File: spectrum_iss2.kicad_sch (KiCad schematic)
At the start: 185 parts, among them IC1 ULA, IC10 4116, IC11 4116, IC12 4116, IC13 4116, IC14 LM1889, IC15 4532, IC16 4532, IC17 4532, IC18 4532, IC19 4532, IC2 Z80, IC20 4532, IC21 4532, IC22 4532, IC23 74LS32, IC24 74LS00, IC25 74LS157, IC26 74LS157, IC3 74LS157, IC4 74LS157, IC5 ROM, IC6 4116, IC7 4116, IC8 4116, IC9 4116, J1 MIC, J2 EAR, J3 EDGE CONNECTOR, J4 Barrel_Jack, T1 COIL 13/39, U1 MODULATOR, U2 L7805, X1 18MHz, X2 4.433MHz

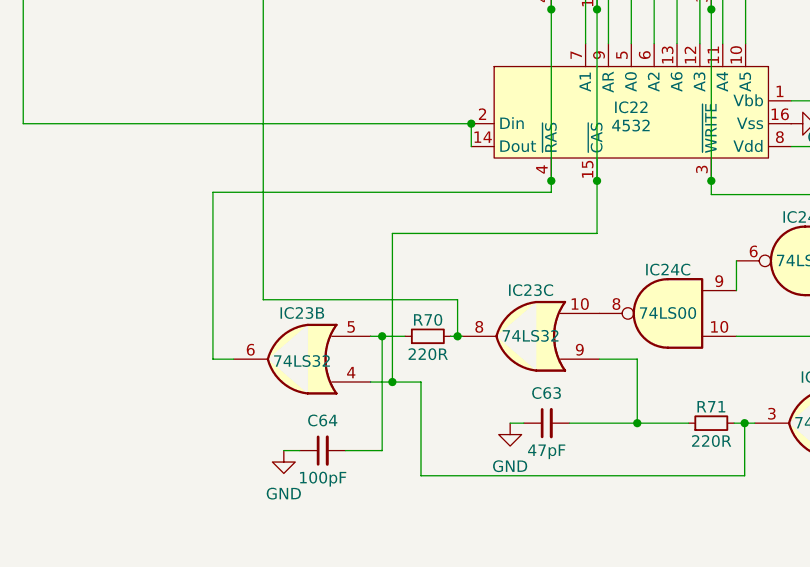
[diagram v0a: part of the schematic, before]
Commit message: fix reversed wiring of RAS and CAS on IC23
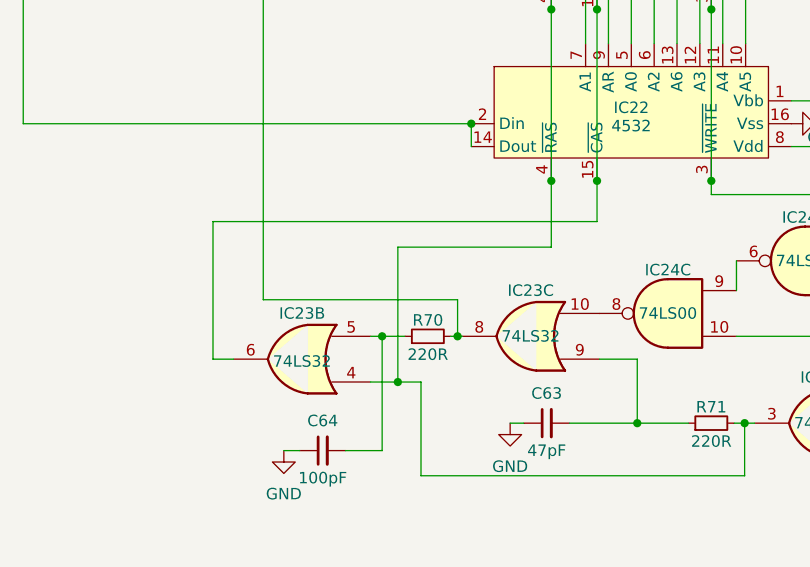
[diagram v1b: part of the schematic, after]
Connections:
- net at IC15.15 (~{CAS}), IC16.15 (~{CAS}), IC17.15 (~{CAS})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: now also IC23.6; no longer IC23.3, IC23.4, R71.2
- net at IC15.4 (~{RAS}), IC16.4 (~{RAS}), IC17.4 (~{RAS})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: now also IC23.3, IC23.4, R71.2; no longer IC23.6
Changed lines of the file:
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@@
   (junction (at 363.728 328.168) (diameter 0) (color 0 0 0 0)
   )
+  (junction (at 571.214 454.406) (diameter 0) (color 0 0 0 0)
+  )
   (junction (at 233.934 203.962) (diameter 0) (color 0 0 0 0)
   )
@@
   (junction (at 467.868 253.238) (diameter 0) (color 0 0 0 0)
   )
-  (junction (at 570.6089 454.406) (diameter 0) (color 0 0 0 0)
-  )
   (junction (at 169.926 271.526) (diameter 0) (color 0 0 0 0)
   )
@@
     (stroke (width 0) (type default))
   )
+  (wire (pts (xy 550.6743 436.5786) (xy 550.6743 451.866))
+    (stroke (width 0) (type default))
+  )
   (wire (pts (xy 535.686 146.812) (xy 535.686 148.844))
     (stroke (width 0) (type default))
@@
     (stroke (width 0) (type default))
   )
-  (wire (pts (xy 570.6089 454.406) (xy 568.198 454.406))
-    (stroke (width 0) (type default))
-  )
   (wire (pts (xy 225.552 255.27) (xy 219.202 255.27))
     (stroke (width 0) (type default))
@@
     (stroke (width 0) (type default))
   )
+  (wire (pts (xy 588.264 432.054) (xy 588.264 439.42))
+    (stroke (width 0) (type default))
+  )
   (wire (pts (xy 614.68 242.57) (xy 614.68 168.402))
     (stroke (width 0) (type default))
   )
+  (wire (pts (xy 571.214 439.42) (xy 571.214 454.406))
+    (stroke (width 0) (type default))
+  )
   (wire (pts (xy 343.408 320.802) (xy 343.408 335.28))
     (stroke (width 0) (type default))
@@
     (stroke (width 0) (type default))
   )
-  (wire (pts (xy 550.672 433.324) (xy 588.264 433.324))
-    (stroke (width 0) (type default))
-  )
   (wire (pts (xy 333.248 305.816) (xy 333.248 320.802))
     (stroke (width 0) (type default))
@@
     (stroke (width 0) (type default))
   )
+  (wire (pts (xy 588.264 439.42) (xy 571.214 439.42))
+    (stroke (width 0) (type default))
+  )
   (wire (pts (xy 225.552 202.184) (xy 225.552 203.962))
     (stroke (width 0) (type default))
@@
     (stroke (width 0) (type default))
   )
+  (wire (pts (xy 593.344 436.5786) (xy 550.6743 436.5786))
+    (stroke (width 0) (type default))
+  )
   (wire (pts (xy 542.036 348.234) (xy 579.374 348.234))
     (stroke (width 0) (type default))
@@
     (stroke (width 0) (type default))
   )
+  (wire (pts (xy 571.214 454.406) (xy 573.786 454.406))
+    (stroke (width 0) (type default))
+  )
   (wire (pts (xy 233.172 226.822) (xy 226.314 226.822))
     (stroke (width 0) (type default))
@@
     (stroke (width 0) (type default))
   )
-  (wire (pts (xy 552.958 451.866) (xy 550.672 451.866))
+  (wire (pts (xy 552.958 451.866) (xy 550.6743 451.866))
     (stroke (width 0) (type default))
   )
@@
     (stroke (width 0) (type default))
   )
-  (wire (pts (xy 570.6089 437.896) (xy 593.344 437.896))
-    (stroke (width 0) (type default))
-  )
   (wire (pts (xy 255.016 191.262) (xy 256.54 191.262))
     (stroke (width 0) (type default))
@@
     (stroke (width 0) (type default))
   )
+  (wire (pts (xy 593.344 436.5786) (xy 593.344 432.054))
+    (stroke (width 0) (type default))
+  )
   (wire (pts (xy 178.816 227.659) (xy 178.816 229.616))
     (stroke (width 0) (type default))
@@
     (stroke (width 0) (type default))
   )
-  (wire (pts (xy 570.6089 454.406) (xy 570.6089 437.896))
-    (stroke (width 0) (type default))
-  )
   (wire (pts (xy 178.816 218.261) (xy 191.516 218.261))
     (stroke (width 0) (type default))
@@
     (stroke (width 0) (type default))
   )
-  (wire (pts (xy 588.264 433.324) (xy 588.264 432.054))
-    (stroke (width 0) (type default))
-  )
   (wire (pts (xy 629.92 173.482) (xy 477.52 173.482))
     (stroke (width 0) (type default))
@@
     (stroke (width 0) (type default))
   )
-  (wire (pts (xy 550.672 451.866) (xy 550.672 433.324))
-    (stroke (width 0) (type default))
-  )
   (wire (pts (xy 201.168 203.962) (xy 225.552 203.962))
     (stroke (width 0) (type default))
@@
     (stroke (width 0) (type default))
   )
-  (wire (pts (xy 593.344 437.896) (xy 593.344 432.054))
-    (stroke (width 0) (type default))
-  )
   (wire (pts (xy 606.044 315.976) (xy 606.044 335.28))
     (stroke (width 0) (type default))
@@
     (stroke (width 0) (type default))
   )
-  (wire (pts (xy 573.786 454.406) (xy 570.6089 454.406))
+  (wire (pts (xy 568.198 454.406) (xy 571.214 454.406))
     (stroke (width 0) (type default))
   )
